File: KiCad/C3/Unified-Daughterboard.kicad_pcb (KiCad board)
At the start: 2 copper layers, 18 x 16.5 mm, 14 parts, among them J1 TYPE-C-31-M12_13, J2 SM04B-SRSS-TB(LF)(SN), U1 TPD4E05U06DQAR

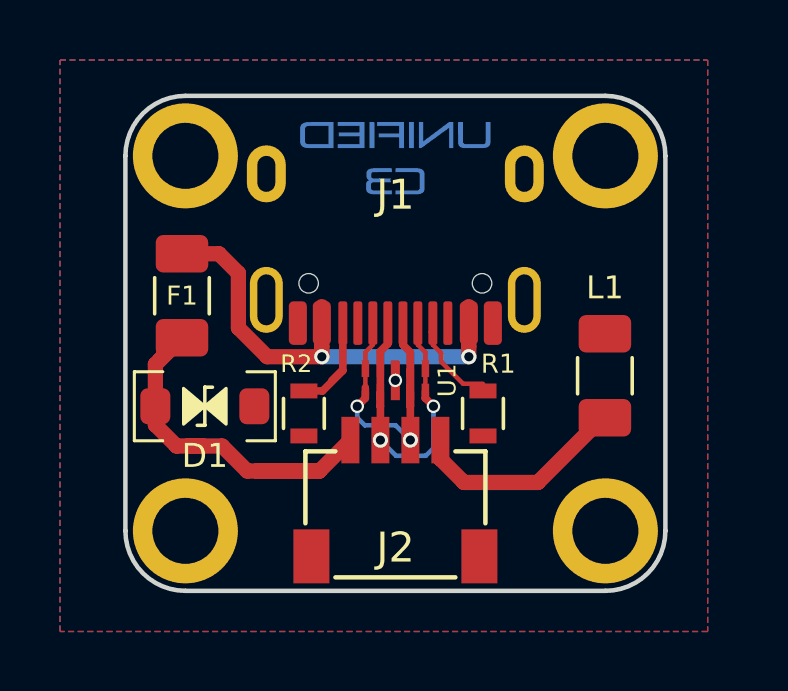
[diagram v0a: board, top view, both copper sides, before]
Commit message: moved the usb outwards
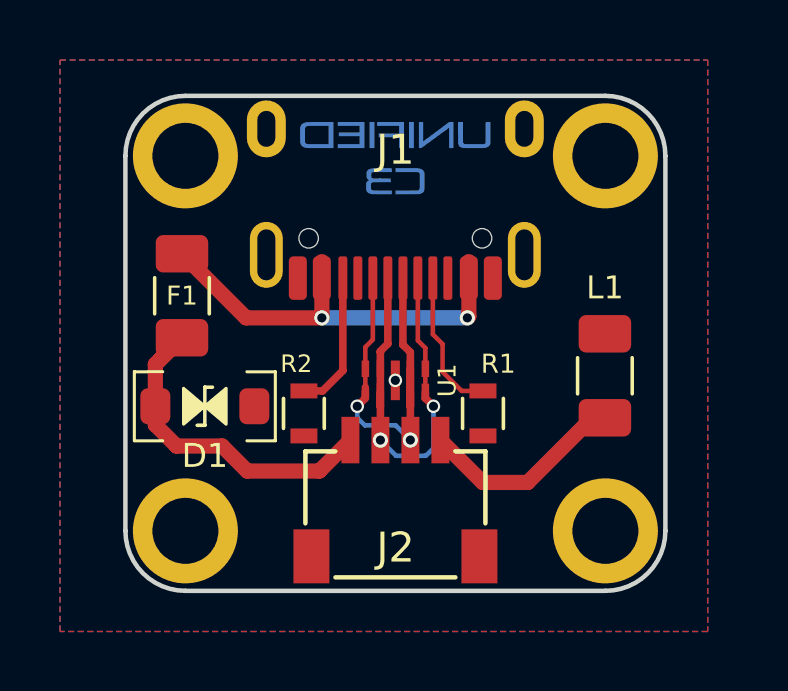
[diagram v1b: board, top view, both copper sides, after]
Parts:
- moved J1 1.50 mm to (75.0, 63.3)
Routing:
- net DA+: track 13.6 -> 16.6 mm
- net DA-: track 13.4 -> 16.4 mm
- net VCC: track 14.7 -> 12.1 mm
- net Net-(J1-PadB5): track 6.33 -> 4.69 mm
- net Net-(J1-PadA5): track 3.84 -> 5.42 mm
- net VBUS: track 15.4 -> 14.2 mm
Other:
- net class Default removed
- net class Power removed
- rule pad_to_mask_clearance: 0.051 -> 0

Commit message: Increased spacing between the mouting holes
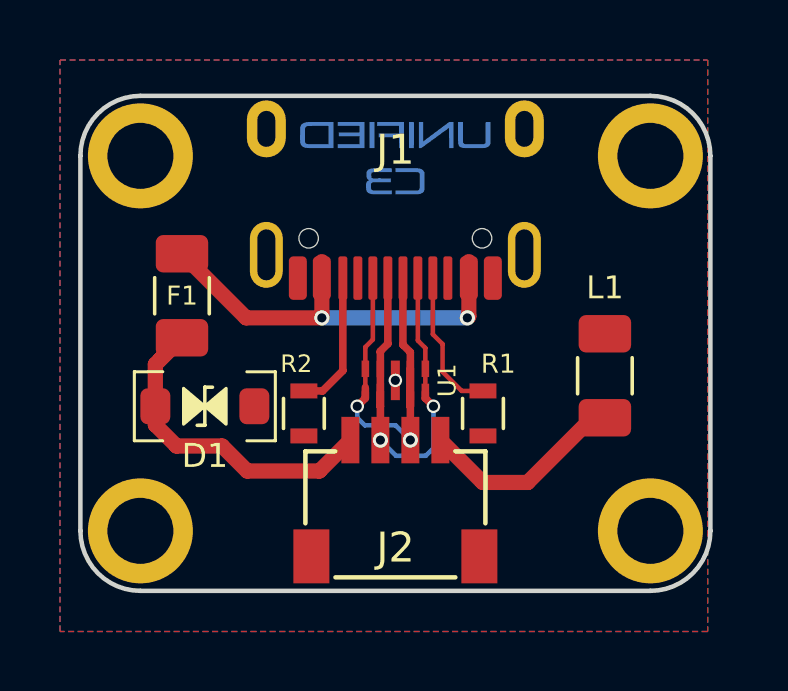
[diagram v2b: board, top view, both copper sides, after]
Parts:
- moved MH1 1.50 mm to (66.5, 58.5)
- moved MH2 1.50 mm to (83.5, 58.5)
- moved MH3 1.50 mm to (66.5, 71.0)
- moved MH4 1.50 mm to (83.5, 71.0)
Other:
- board size 18 x 16.5 mm -> 21 x 16.5 mm
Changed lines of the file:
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@@
   (net 10 "VBUS")
   (footprint "random-keyboard-parts:Generic-Mounthole" (layer "F.Cu")
-    (at 82.0045 58.543)
+    (at 83.5045 58.543)
     (attr exclude_from_pos_files exclude_from_bom)
     (fp_text reference "MH2" (at 0 2) (layer "Dwgs.User") hide
@@
   )
   (footprint "random-keyboard-parts:Generic-Mounthole" (layer "F.Cu")
-    (at 68.0045 58.543)
+    (at 66.5045 58.543)
     (attr exclude_from_pos_files exclude_from_bom)
     (fp_text reference "MH1" (at 0 2) (layer "Dwgs.User")
@@
   )
   (footprint "random-keyboard-parts:Generic-Mounthole" (layer "F.Cu")
-    (at 82.0045 71.043)
+    (at 83.5045 71.043)
     (attr exclude_from_pos_files exclude_from_bom)
     (fp_text reference "MH4" (at 0 2) (layer "Dwgs.User") hide
@@
   )
   (footprint "random-keyboard-parts:Generic-Mounthole" (layer "F.Cu")
-    (at 68.0045 71.043)
+    (at 66.5045 71.043)
     (attr exclude_from_pos_files exclude_from_bom)
     (fp_text reference "MH3" (at 0 2) (layer "Dwgs.User") hide
@@
       (xy 0.003836 4.881129)) (layer "B.Mask") (width 0) (fill solid))
   )
-  (gr_line (start 84.0045 58.543) (end 84.0045 71.043) (layer "Edge.Cuts") (width 0.15))
-  (gr_arc (start 82.0045 71.043) (end 82.0045 73.043) (angle -90) (layer "Edge.Cuts") (width 0.15))
-  (gr_arc (start 82.0045 58.543) (end 84.0045 58.543) (angle -90) (layer "Edge.Cuts") (width 0.15))
-  (gr_arc (start 68.0045 71.043) (end 66.0045 71.043) (angle -90) (layer "Edge.Cuts") (width 0.15))
-  (gr_arc (start 68.0045 58.543) (end 68.0045 56.543) (angle -90) (layer "Edge.Cuts") (width 0.15))
-  (gr_line (start 68.0045 56.543) (end 82.0045 56.543) (layer "Edge.Cuts") (width 0.15))
-  (gr_line (start 66.0045 71.043) (end 66.0045 58.543) (layer "Edge.Cuts") (width 0.15))
-  (gr_line (start 82.0045 73.043) (end 68.0045 73.043) (layer "Edge.Cuts") (width 0.15))
+  (gr_line (start 85.5045 58.543) (end 85.5045 71.043) (layer "Edge.Cuts") (width 0.15))
+  (gr_arc (start 83.504501 71.043) (end 83.5045 73.043) (angle -90) (layer "Edge.Cuts") (width 0.15))
+  (gr_arc (start 83.5045 58.542999) (end 85.5045 58.543) (angle -90) (layer "Edge.Cuts") (width 0.15))
+  (gr_arc (start 66.5045 71.043001) (end 64.5045 71.043) (angle -90) (layer "Edge.Cuts") (width 0.15))
+  (gr_arc (start 66.504499 58.543) (end 66.5045 56.543) (angle -90) (layer "Edge.Cuts") (width 0.15))
+  (gr_line (start 66.5045 56.543) (end 83.5045 56.543) (layer "Edge.Cuts") (width 0.15))
+  (gr_line (start 64.5045 71.043) (end 64.5045 58.543) (layer "Edge.Cuts") (width 0.15))
+  (gr_line (start 83.5045 73.043) (end 66.5045 73.043) (layer "Edge.Cuts") (width 0.15))
   (gr_line (start 73.0045 68.543) (end 73.0045 67.043) (layer "F.CrtYd") (width 0.05))
   (gr_line (start 78.0045 72.543) (end 72.0045 72.543) (layer "F.CrtYd") (width 0.05))
@@
   )
   (dimension (type aligned) (layer "Dwgs.User")
-    (pts (xy 68.0045 56.543) (xy 82.0045 56.543))
+    (pts (xy 66.504499 58.543) (xy 83.5045 58.542999))
     (height -7.499999)
-    (gr_text "14.0000 mm" (at 75.0045 47.443001) (layer "Dwgs.User")
+    (gr_text "17,0000 mm" (at 75.004499 49.443001) (layer "Dwgs.User")
       (effects (font (size 1.5 1.5) (thickness 0.1)))
     )
@@
   )
   (dimension (type aligned) (layer "Dwgs.User")
-    (pts (xy 84.0045 56.543) (xy 66.0045 56.543))
+    (pts (xy 85.5045 58.543) (xy 64.5045 58.543))
     (height 14)
-    (gr_text "18.0000 mm" (at 75.0045 40.943) (layer "Dwgs.User")
+    (gr_text "21,0000 mm" (at 75.0045 42.943) (layer "Dwgs.User")
       (effects (font (size 1.5 1.5) (thickness 0.1)))
     )

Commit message: Increased x spacing between mounting points to 18mm
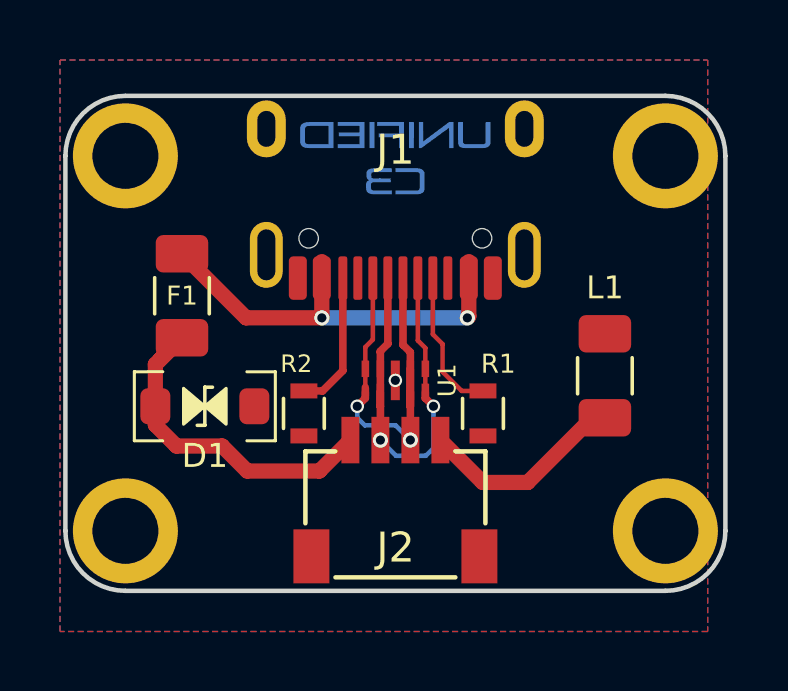
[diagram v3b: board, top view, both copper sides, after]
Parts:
- moved MH1 0.50 mm to (66.0, 58.5)
- moved MH2 0.50 mm to (84.0, 58.5)
- moved MH3 0.50 mm to (66.0, 71.0)
- moved MH4 0.50 mm to (84.0, 71.0)
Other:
- board size 21 x 16.5 mm -> 22 x 16.5 mm
